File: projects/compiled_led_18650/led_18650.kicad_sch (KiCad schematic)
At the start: 3 parts

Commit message: F5: human-quality pass — weld, route beauty, silent flags, design guide
The user's mandate: schematics must read as hand-drawn — tidy wires over
tag pairs, clean corners, nothing on screen but symbol, model and value.

- internal/place2/weld: same-net label islands get welded into real wires
  (straight/L/Z) whenever a clean corridor exists; every candidate is
  validated against gate.Check and reverted on any new violation. Redundant
  labels removed, one kept as documentation.
- routeNets beauty policy: a path with more than 3 bends or >70% detour
  over Manhattan distance reads worse than a label — demoted before it is
  ever drawn. Combined with weld this replaces snakes with short wires.
- PWR_FLAG value text hidden (sexp.HidePropertyText): the flag exists for
  ERC, not for the reader.
- design_guide: human-schematic conventions (signal flow, wire-vs-label,
  spacing recipes in grid cells, iteration protocol) distilled from
  SparkFun/KLC/IEEE-315/Altium/H&H research, embedded in the binary and
  served as an MCP tool for authoring LLMs.
- Crystal clusters reworked in both MCU sources: vertical crystal, straight
  XTAL1, single-L XTAL2, horizontal load caps — full Pierce oscillator
  wiring, zero label pairs. NE555 timing chain now fully wired via weld.

Co-Authored-By: Claude Fable 5 <noreply@anthropic.com>
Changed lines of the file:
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@@
     (instances
       (project ""
-        (path "/ca345edc-8eb3-4489-85fb-c4c12b43cbf1" (reference "BT1") (unit 1)))))
+        (path "/dd3cde3c-46a0-464b-84a0-c76ee9592728" (reference "BT1") (unit 1)))))
   (symbol (lib_id "Device:R")
     (at 41.91 27.94 90) (unit 1) (exclude_from_sim no) (in_bom yes) (on_board yes) (dnp no)
@@
     (instances
       (project ""
-        (path "/ca345edc-8eb3-4489-85fb-c4c12b43cbf1" (reference "R1") (unit 1)))))
+        (path "/dd3cde3c-46a0-464b-84a0-c76ee9592728" (reference "R1") (unit 1)))))
   (symbol (lib_id "Device:LED")
     (at 53.34 31.75 90) (unit 1) (exclude_from_sim no) (in_bom yes) (on_board yes) (dnp no)
@@
     (instances
       (project ""
-        (path "/ca345edc-8eb3-4489-85fb-c4c12b43cbf1" (reference "D1") (unit 1)))))
+        (path "/dd3cde3c-46a0-464b-84a0-c76ee9592728" (reference "D1") (unit 1)))))
   (wire
     (pts (xy 53.34 27.94) (xy 45.72 27.94))
@@
     (instances
       (project ""
-        (path "/ca345edc-8eb3-4489-85fb-c4c12b43cbf1" (reference "#PWR01") (unit 1)))))
+        (path "/dd3cde3c-46a0-464b-84a0-c76ee9592728" (reference "#PWR01") (unit 1)))))
   (wire
     (pts (xy 53.34 35.56) (xy 53.34 38.1))
@@
     (instances
       (project ""
-        (path "/ca345edc-8eb3-4489-85fb-c4c12b43cbf1" (reference "#PWR02") (unit 1)))))
+        (path "/dd3cde3c-46a0-464b-84a0-c76ee9592728" (reference "#PWR02") (unit 1)))))
   (wire
     (pts (xy 27.94 35.56) (xy 27.94 38.1))
@@
         (font (size 1.27 1.27)) (hide yes)))
     (property "Value" "PWR_FLAG"
-      (at 16.39 35.56 0)
+      (at 25.4 38.1 0)
       (effects
-        (font (size 1.27 1.27))))
+        (font (size 1.27 1.27)) (hide yes)))
     (property "Footprint" ""
       (at 25.4 35.56 0)
@@
     (instances
       (project ""
-        (path "/ca345edc-8eb3-4489-85fb-c4c12b43cbf1" (reference "#FLG01") (unit 1)))))
+        (path "/dd3cde3c-46a0-464b-84a0-c76ee9592728" (reference "#FLG01") (unit 1)))))
   (wire
     (pts (xy 27.94 35.56) (xy 25.4 35.56))

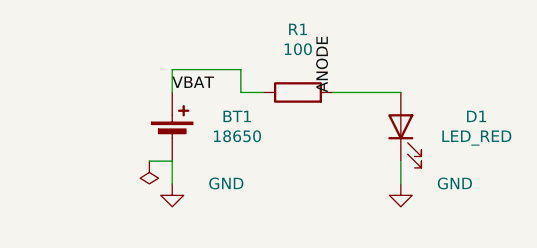
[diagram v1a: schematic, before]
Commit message: Body model sees real symbol graphics; quiet nets drop junction tags
User-reported flaws from visual review, both fixed at the root:

- Wires over symbol artwork: the body model was pin-derived and blind to
  drawn graphics — an op-amp triangle's vertices stick out beyond the pin
  box, so "legal" wires crossed the drawing. internal/sexp/graphics.go now
  parses rectangle/polyline/circle/arc/bezier extents per unit with the
  exact pin transform; metrics.BodyBBox unions them with the legacy box,
  clamped off pin tips (Device:LED's emission arrows overhang the cathode
  pin and would have swallowed it). NE5532 feedback: 8 stroke crossings
  through the triangle before, 0 after (loops now label pairs). The model
  also exposed genuinely bad baked geometry in mcu_minimal_atmega328's
  crystal — repositioned with the template contract intact.

- "ANODE" tag on a resistor leg: net names with a "_" prefix are now
  quiet — connectivity only, their documentation label is stripped at the
  end of compilation when the wiring alone keeps the net whole. Junction
  nodes (R->LED) stay unlabeled like in any hand-drawn schematic.

- Battery hump: led_18650 anchors R1 in the pin's exit direction; the
  design guide gains the "respect the pin's exit direction" and "internal
  junctions carry no tag" recipes.

Co-Authored-By: Claude Fable 5 <noreply@anthropic.com>
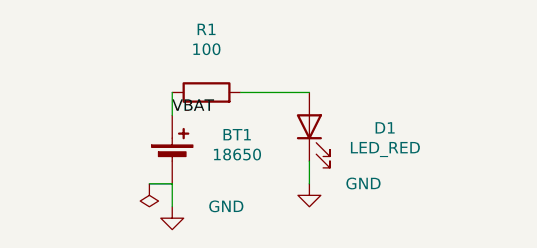
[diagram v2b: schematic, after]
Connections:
- net ANODE: no longer names the net of D1.2 (A), R1.2
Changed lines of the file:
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@@
     (path "/" (page "1")))
   (symbol (lib_id "Device:Battery_Cell")
-    (at 27.94 33.02 0) (unit 1) (exclude_from_sim no) (in_bom yes) (on_board yes) (dnp no)
+    (at 27.94 35.56 0) (unit 1) (exclude_from_sim no) (in_bom yes) (on_board yes) (dnp no)
     (property "Reference" "BT1"
-      (at 35.15 30.65 0)
+      (at 35.15 32.68 0)
       (effects
         (font (size 1.27 1.27))))
     (property "Value" "18650"
-      (at 35.15 32.85 0)
+      (at 35.15 34.88 0)
       (effects
         (font (size 1.27 1.27))))
     (property "Footprint" ""
-      (at 27.94 33.02 0)
+      (at 27.94 35.56 0)
       (effects
         (font (size 1.27 1.27)) (hide yes)))
     (property "Datasheet" ""
-      (at 27.94 33.02 0)
+      (at 27.94 35.56 0)
       (effects
         (font (size 1.27 1.27)) (hide yes)))
     (property "Description" ""
-      (at 27.94 33.02 0)
+      (at 27.94 35.56 0)
       (effects
         (font (size 1.27 1.27)) (hide yes)))
@@
     (instances
       (project ""
-        (path "/dd3cde3c-46a0-464b-84a0-c76ee9592728" (reference "BT1") (unit 1)))))
+        (path "/a69aab39-a8a8-4935-aa47-6a81263334ac" (reference "BT1") (unit 1)))))
   (symbol (lib_id "Device:R")
-    (at 41.91 27.94 90) (unit 1) (exclude_from_sim no) (in_bom yes) (on_board yes) (dnp no)
+    (at 31.75 27.94 90) (unit 1) (exclude_from_sim no) (in_bom yes) (on_board yes) (dnp no)
     (property "Reference" "R1"
-      (at 41.91 20.98 90)
+      (at 31.75 20.98 90)
       (effects
         (font (size 1.27 1.27))))
     (property "Value" "100"
-      (at 41.91 23.18 90)
+      (at 31.75 23.18 90)
       (effects
         (font (size 1.27 1.27))))
     (property "Footprint" ""
-      (at 41.91 27.94 0)
+      (at 31.75 27.94 0)
       (effects
         (font (size 1.27 1.27)) (hide yes)))
     (property "Datasheet" ""
-      (at 41.91 27.94 0)
+      (at 31.75 27.94 0)
       (effects
         (font (size 1.27 1.27)) (hide yes)))
     (property "Description" ""
-      (at 41.91 27.94 0)
+      (at 31.75 27.94 0)
       (effects
         (font (size 1.27 1.27)) (hide yes)))
@@
     (instances
       (project ""
-        (path "/dd3cde3c-46a0-464b-84a0-c76ee9592728" (reference "R1") (unit 1)))))
+        (path "/a69aab39-a8a8-4935-aa47-6a81263334ac" (reference "R1") (unit 1)))))
   (symbol (lib_id "Device:LED")
-    (at 53.34 31.75 90) (unit 1) (exclude_from_sim no) (in_bom yes) (on_board yes) (dnp no)
+    (at 43.18 31.75 90) (unit 1) (exclude_from_sim no) (in_bom yes) (on_board yes) (dnp no)
     (property "Reference" "D1"
-      (at 61.75 30.65 90)
+      (at 51.59 31.92 90)
       (effects
         (font (size 1.27 1.27))))
     (property "Value" "LED_RED"
-      (at 61.75 32.85 90)
+      (at 51.59 34.12 90)
       (effects
         (font (size 1.27 1.27))))
     (property "Footprint" ""
-      (at 53.34 31.75 0)
+      (at 43.18 31.75 0)
       (effects
         (font (size 1.27 1.27)) (hide yes)))
     (property "Datasheet" ""
-      (at 53.34 31.75 0)
+      (at 43.18 31.75 0)
       (effects
         (font (size 1.27 1.27)) (hide yes)))
     (property "Description" ""
-      (at 53.34 31.75 0)
+      (at 43.18 31.75 0)
       (effects
         (font (size 1.27 1.27)) (hide yes)))
@@
     (instances
       (project ""
-        (path "/dd3cde3c-46a0-464b-84a0-c76ee9592728" (reference "D1") (unit 1)))))
+        (path "/a69aab39-a8a8-4935-aa47-6a81263334ac" (reference "D1") (unit 1)))))
   (wire
-    (pts (xy 53.34 27.94) (xy 45.72 27.94))
+    (pts (xy 43.18 27.94) (xy 35.56 27.94))
     (stroke (width 0) (type default)))
-  (label "ANODE"
-    (at 45.72 27.94 90) (fields_autoplaced yes)
-    (effects
-      (font (size 1.27 1.27)) (justify left bottom))
-    (property "Intersheet References" ""
-      (at 0 0 0)
-      (effects
-        (font (size 1.27 1.27)) (hide yes))))
   (symbol (lib_id "power:GND")
-    (at 53.34 38.1 0) (unit 1) (exclude_from_sim no) (in_bom no) (on_board no) (dnp no)
+    (at 43.18 38.1 0) (unit 1) (exclude_from_sim no) (in_bom no) (on_board no) (dnp no)
     (property "Reference" "#PWR01"
-      (at 53.34 38.1 0)
+      (at 43.18 38.1 0)
       (effects
         (font (size 1.27 1.27)) (hide yes)))
     (property "Value" "GND"
-      (at 59.35 38.1 0)
+      (at 49.19 38.1 0)
       (effects
         (font (size 1.27 1.27))))
     (property "Footprint" ""
-      (at 53.34 38.1 0)
+      (at 43.18 38.1 0)
       (effects
         (font (size 1.27 1.27)) (hide yes)))
     (property "Datasheet" ""
-      (at 53.34 38.1 0)
+      (at 43.18 38.1 0)
       (effects
         (font (size 1.27 1.27)) (hide yes)))
     (property "Description" ""
-      (at 53.34 38.1 0)
+      (at 43.18 38.1 0)
       (effects
         (font (size 1.27 1.27)) (hide yes)))
@@
     (instances
       (project ""
-        (path "/dd3cde3c-46a0-464b-84a0-c76ee9592728" (reference "#PWR01") (unit 1)))))
+        (path "/a69aab39-a8a8-4935-aa47-6a81263334ac" (reference "#PWR01") (unit 1)))))
   (wire
-    (pts (xy 53.34 35.56) (xy 53.34 38.1))
+    (pts (xy 43.18 35.56) (xy 43.18 38.1))
     (stroke (width 0) (type default)))
   (symbol (lib_id "power:GND")
-    (at 27.94 38.1 0) (unit 1) (exclude_from_sim no) (in_bom no) (on_board no) (dnp no)
+    (at 27.94 40.64 0) (unit 1) (exclude_from_sim no) (in_bom no) (on_board no) (dnp no)
     (property "Reference" "#PWR02"
-      (at 27.94 38.1 0)
+      (at 27.94 40.64 0)
       (effects
         (font (size 1.27 1.27)) (hide yes)))
     (property "Value" "GND"
-      (at 33.95 38.1 0)
+      (at 33.95 40.64 0)
       (effects
         (font (size 1.27 1.27))))
     (property "Footprint" ""
-      (at 27.94 38.1 0)
+      (at 27.94 40.64 0)
       (effects
         (font (size 1.27 1.27)) (hide yes)))
     (property "Datasheet" ""
-      (at 27.94 38.1 0)
+      (at 27.94 40.64 0)
       (effects
         (font (size 1.27 1.27)) (hide yes)))
     (property "Description" ""
-      (at 27.94 38.1 0)
+      (at 27.94 40.64 0)
       (effects
         (font (size 1.27 1.27)) (hide yes)))
@@
     (instances
       (project ""
-        (path "/dd3cde3c-46a0-464b-84a0-c76ee9592728" (reference "#PWR02") (unit 1)))))
+        (path "/a69aab39-a8a8-4935-aa47-6a81263334ac" (reference "#PWR02") (unit 1)))))
   (wire
-    (pts (xy 27.94 35.56) (xy 27.94 38.1))
+    (pts (xy 27.94 38.1) (xy 27.94 40.64))
     (stroke (width 0) (type default)))
   (wire
-    (pts (xy 27.94 27.94) (xy 27.94 25.4))
-    (stroke (width 0) (type default)))
-  (wire
-    (pts (xy 27.94 25.4) (xy 35.56 25.4))
-    (stroke (width 0) (type default)))
-  (wire
-    (pts (xy 35.56 25.4) (xy 35.56 27.94))
-    (stroke (width 0) (type default)))
-  (wire
-    (pts (xy 35.56 27.94) (xy 38.1 27.94))
+    (pts (xy 27.94 30.48) (xy 27.94 27.94))
     (stroke (width 0) (type default)))
   (label "VBAT"
-    (at 27.94 27.94 0) (fields_autoplaced yes)
+    (at 27.94 30.48 180) (fields_autoplaced yes)
     (effects
       (font (size 1.27 1.27)) (justify left bottom))
@@
         (font (size 1.27 1.27)) (hide yes))))
   (symbol (lib_id "power:PWR_FLAG")
-    (at 25.4 35.56 180) (unit 1) (exclude_from_sim no) (in_bom no) (on_board no) (dnp no)
+    (at 25.4 38.1 180) (unit 1) (exclude_from_sim no) (in_bom no) (on_board no) (dnp no)
     (property "Reference" "#FLG01"
-      (at 25.4 35.56 0)
+      (at 25.4 38.1 0)
       (effects
         (font (size 1.27 1.27)) (hide yes)))
     (property "Value" "PWR_FLAG"
+      (at 25.4 40.64 0)
+      (effects
+        (font (size 1.27 1.27)) (hide yes)))
+    (property "Footprint" ""
       (at 25.4 38.1 0)
       (effects
         (font (size 1.27 1.27)) (hide yes)))
-    (property "Footprint" ""
-      (at 25.4 35.56 0)
-      (effects
-        (font (size 1.27 1.27)) (hide yes)))
     (property "Datasheet" ""
-      (at 25.4 35.56 0)
+      (at 25.4 38.1 0)
       (effects
         (font (size 1.27 1.27)) (hide yes)))
     (property "Description" ""
-      (at 25.4 35.56 0)
+      (at 25.4 38.1 0)
       (effects
         (font (size 1.27 1.27)) (hide yes)))
@@
     (instances
       (project ""
-        (path "/dd3cde3c-46a0-464b-84a0-c76ee9592728" (reference "#FLG01") (unit 1)))))
+        (path "/a69aab39-a8a8-4935-aa47-6a81263334ac" (reference "#FLG01") (unit 1)))))
   (wire
-    (pts (xy 27.94 35.56) (xy 25.4 35.56))
+    (pts (xy 27.94 38.1) (xy 25.4 38.1))
     (stroke (width 0) (type default))))
